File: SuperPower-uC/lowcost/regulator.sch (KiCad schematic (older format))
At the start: 23 parts, among them Q5 AO3401A, Q6 AO3401A, Q7 2N7002, U10 FP6291LR, U11 ME6210A33P, U12 ME6210A33P

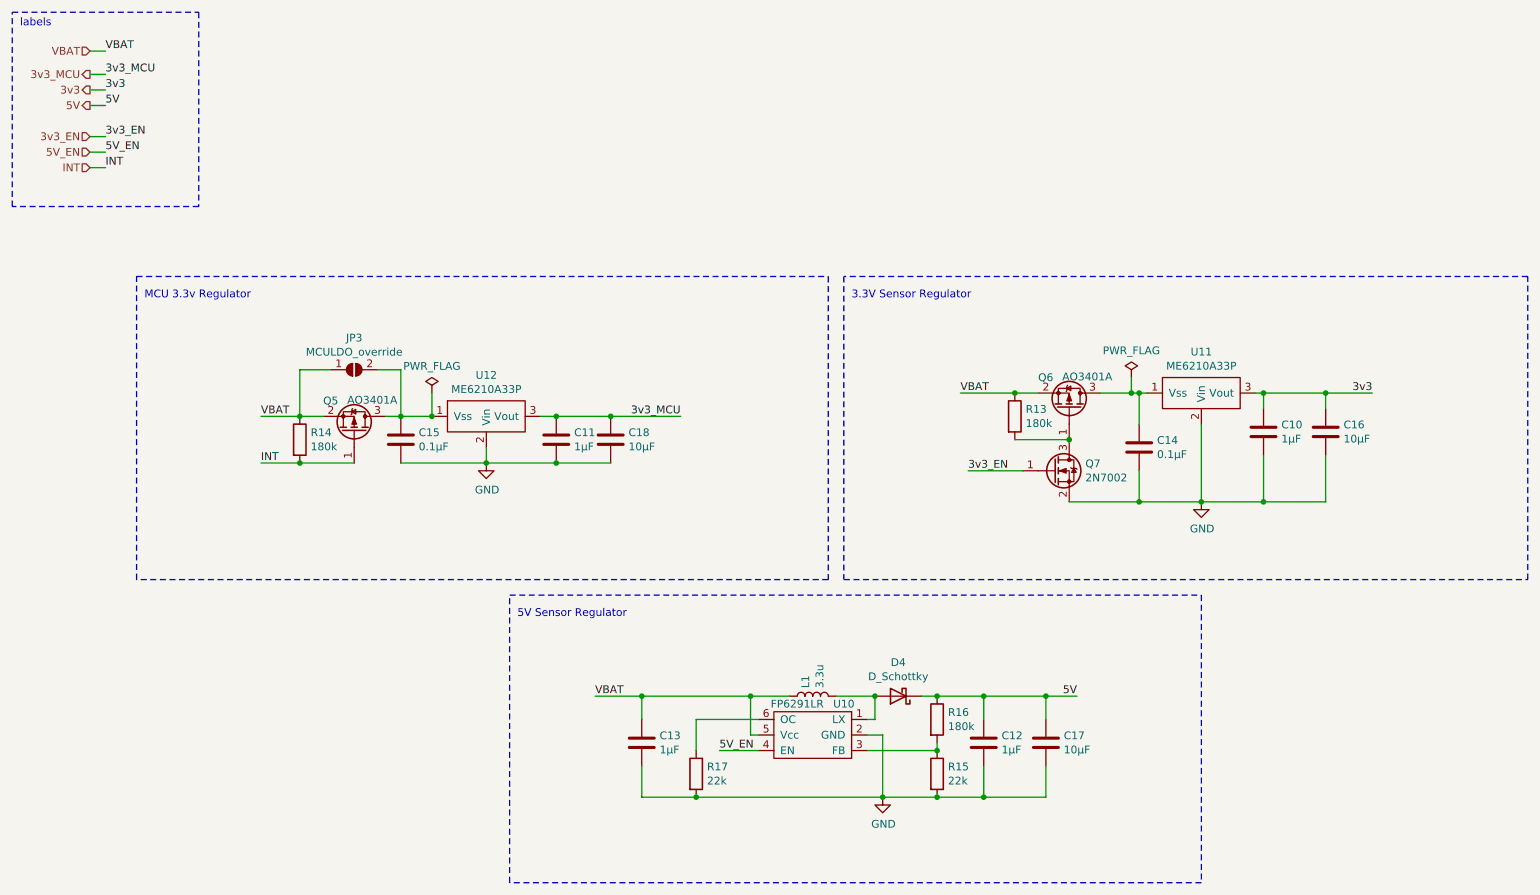
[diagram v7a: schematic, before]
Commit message: added 100R to protection ic and some minor other stuff
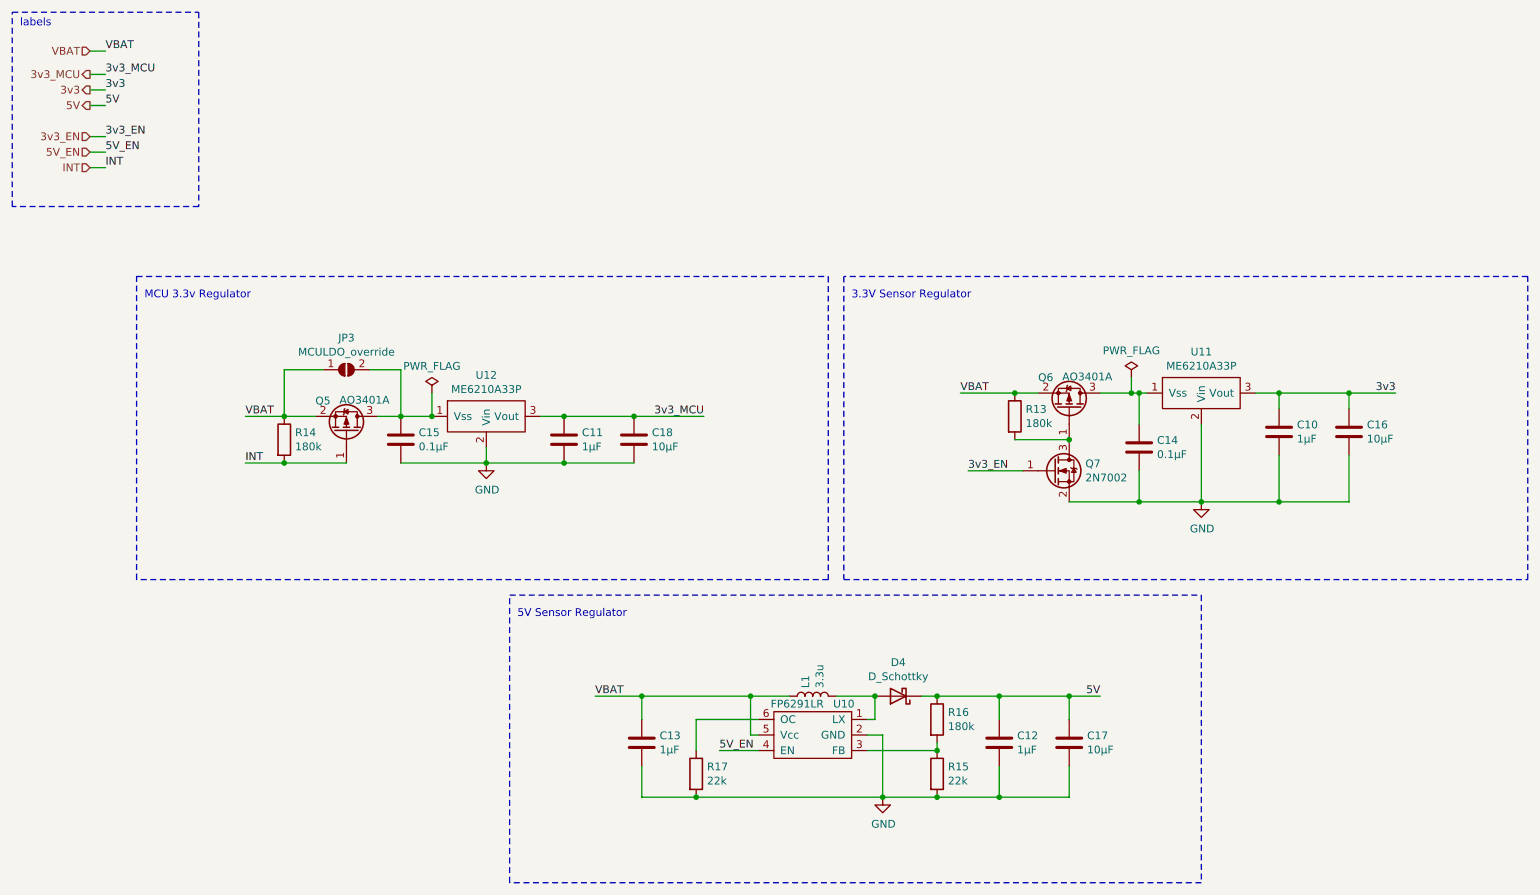
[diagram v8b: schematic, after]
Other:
- moved on the sheet: C10, C11, C12, C16, C17, C18, JP3, Q5, R14
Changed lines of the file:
@@
 L Transistor_FET:AO3401A Q5
 U 1 1 5F80895A
-P 2800 3300
-F 0 "Q5" V 3000 3100 50  0000 L CNN
-F 1 "AO3401A" V 3005 3255 50  0000 L CNN
-F 2 "Package_TO_SOT_SMD:SOT-23_Handsoldering" H 3000 3225 50  0001 L CIN
-F 3 "http://www.aosmd.com/pdfs/datasheet/AO3401A.pdf" H 2800 3300 50  0001 L CNN
-F 4 "C347476" H 2800 3300 50  0001 C CNN "LCSC"
-	1    2800 3300
+P 2750 3300
+F 0 "Q5" V 2950 3100 50  0000 L CNN
+F 1 "AO3401A" V 2955 3255 50  0000 L CNN
+F 2 "Package_TO_SOT_SMD:SOT-23_Handsoldering" H 2950 3225 50  0001 L CIN
+F 3 "http://www.aosmd.com/pdfs/datasheet/AO3401A.pdf" H 2750 3300 50  0001 L CNN
+F 4 "C347476" H 2750 3300 50  0001 C CNN "LCSC"
+	1    2750 3300
 	0    1    -1   0
 $EndComp
@@
 $EndComp
 Wire Wire Line
-	3000 3200 3100 3200
+	2950 3200 3100 3200
 Wire Wire Line
 	7600 3050 7800 3050
@@
 L Device:R R14
 U 1 1 5F8145C2
-P 2450 3350
-F 0 "R14" H 2520 3396 50  0000 L CNN
-F 1 "180k" H 2520 3305 50  0000 L CNN
-F 2 "Resistor_SMD:R_0603_1608Metric_Pad1.05x0.95mm_HandSolder" V 2380 3350 50  0001 C CNN
-F 3 "~" H 2450 3350 50  0001 C CNN
-F 4 "C22827" H 2450 3350 50  0001 C CNN "LCSC"
-	1    2450 3350
-	1    0    0    -1
-$EndComp
-Wire Wire Line
-	2600 3200 2450 3200
+P 2350 3350
+F 0 "R14" H 2420 3396 50  0000 L CNN
+F 1 "180k" H 2420 3305 50  0000 L CNN
+F 2 "Resistor_SMD:R_0603_1608Metric_Pad1.05x0.95mm_HandSolder" V 2280 3350 50  0001 C CNN
+F 3 "~" H 2350 3350 50  0001 C CNN
+F 4 "C22827" H 2350 3350 50  0001 C CNN "LCSC"
+	1    2350 3350
+	1    0    0    -1
+$EndComp
+Wire Wire Line
+	2550 3200 2350 3200
 $Comp
 L Transistor_FET:2N7002 Q7
@@
 L Device:C C10
 U 1 1 5F81F790
-P 8650 3300
-F 0 "C10" H 8765 3346 50  0000 L CNN
-F 1 "1µF" H 8765 3255 50  0000 L CNN
-F 2 "Capacitor_SMD:C_0603_1608Metric_Pad1.05x0.95mm_HandSolder" H 8688 3150 50  0001 C CNN
-F 3 "~" H 8650 3300 50  0001 C CNN
-F 4 "C15849" H 8650 3300 50  0001 C CNN "LCSC"
-	1    8650 3300
+P 8750 3300
+F 0 "C10" H 8865 3346 50  0000 L CNN
+F 1 "1µF" H 8865 3255 50  0000 L CNN
+F 2 "Capacitor_SMD:C_0603_1608Metric_Pad1.05x0.95mm_HandSolder" H 8788 3150 50  0001 C CNN
+F 3 "~" H 8750 3300 50  0001 C CNN
+F 4 "C15849" H 8750 3300 50  0001 C CNN "LCSC"
+	1    8750 3300
 	1    0    0    -1
 $EndComp
@@
 L Device:C C11
 U 1 1 5F822A09
-P 4100 3350
-F 0 "C11" H 4215 3396 50  0000 L CNN
-F 1 "1µF" H 4215 3305 50  0000 L CNN
-F 2 "Capacitor_SMD:C_0603_1608Metric_Pad1.05x0.95mm_HandSolder" H 4138 3200 50  0001 C CNN
-F 3 "~" H 4100 3350 50  0001 C CNN
-F 4 "C15849" H 4100 3350 50  0001 C CNN "LCSC"
-	1    4100 3350
-	1    0    0    -1
-$EndComp
-Connection ~ 4100 3200
-Wire Wire Line
-	4100 3200 4000 3200
-Wire Wire Line
-	4100 3500 3650 3500
+P 4150 3350
+F 0 "C11" H 4265 3396 50  0000 L CNN
+F 1 "1µF" H 4265 3305 50  0000 L CNN
+F 2 "Capacitor_SMD:C_0603_1608Metric_Pad1.05x0.95mm_HandSolder" H 4188 3200 50  0001 C CNN
+F 3 "~" H 4150 3350 50  0001 C CNN
+F 4 "C15849" H 4150 3350 50  0001 C CNN "LCSC"
+	1    4150 3350
+	1    0    0    -1
+$EndComp
+Connection ~ 4150 3200
 $Comp
 L Device:C C14
@@
 Wire Wire Line
 	7850 3750 7400 3750
-Connection ~ 2450 3200
-Wire Wire Line
-	2950 2900 3100 2900
+Connection ~ 2350 3200
+Wire Wire Line
+	2900 2900 3100 2900
 $Comp
 L Jumper:SolderJumper_2_Open JP3
 U 1 1 5F81FE3B
-P 2800 2900
-F 0 "JP3" H 2800 3105 50  0000 C CNN
-F 1 "MCULDO_override" H 2800 3014 50  0000 C CNN
-F 2 "Jumper:SolderJumper-2_P1.3mm_Open_Pad1.0x1.5mm" H 2800 2900 50  0001 C CNN
-F 3 "~" H 2800 2900 50  0001 C CNN
-	1    2800 2900
-	1    0    0    -1
-$EndComp
-Wire Wire Line
-	2450 2900 2450 3200
+P 2750 2900
+F 0 "JP3" H 2750 3105 50  0000 C CNN
+F 1 "MCULDO_override" H 2750 3014 50  0000 C CNN
+F 2 "Jumper:SolderJumper-2_P1.3mm_Open_Pad1.0x1.5mm" H 2750 2900 50  0001 C CNN
+F 3 "~" H 2750 2900 50  0001 C CNN
+	1    2750 2900
+	1    0    0    -1
+$EndComp
+Wire Wire Line
+	2350 2900 2350 3200
 Wire Wire Line
 	3100 2900 3100 3200
 Wire Wire Line
-	2450 2900 2650 2900
+	2350 2900 2600 2900
 $Comp
 L Device:C C16
 U 1 1 5F868BFD
-P 9050 3300
-F 0 "C16" H 9165 3346 50  0000 L CNN
-F 1 "10µF" H 9165 3255 50  0000 L CNN
-F 2 "Capacitor_SMD:C_0603_1608Metric_Pad1.05x0.95mm_HandSolder" H 9088 3150 50  0001 C CNN
-F 3 "~" H 9050 3300 50  0001 C CNN
-F 4 "C19702" H 9050 3300 50  0001 C CNN "LCSC"
-	1    9050 3300
+P 9200 3300
+F 0 "C16" H 9315 3346 50  0000 L CNN
+F 1 "10µF" H 9315 3255 50  0000 L CNN
+F 2 "Capacitor_SMD:C_0603_1608Metric_Pad1.05x0.95mm_HandSolder" H 9238 3150 50  0001 C CNN
+F 3 "~" H 9200 3300 50  0001 C CNN
+F 4 "C19702" H 9200 3300 50  0001 C CNN "LCSC"
+	1    9200 3300
 	1    0    0    -1
 $EndComp
@@
 	8250 3250 8250 3750
 Wire Wire Line
-	8250 3750 8650 3750
-Wire Wire Line
-	8600 3050 8650 3050
-Wire Wire Line
-	8650 3050 8650 3150
-Connection ~ 8650 3050
-Wire Wire Line
-	8650 3050 9050 3050
-Wire Wire Line
-	9050 3050 9050 3150
-Connection ~ 9050 3050
-Wire Wire Line
-	8650 3450 8650 3750
-Connection ~ 8650 3750
-Wire Wire Line
-	8650 3750 9050 3750
-Wire Wire Line
-	9050 3450 9050 3750
+	8250 3750 8750 3750
+Wire Wire Line
+	8600 3050 8750 3050
+Wire Wire Line
+	8750 3050 8750 3150
+Connection ~ 8750 3050
+Wire Wire Line
+	8750 3050 9200 3050
+Wire Wire Line
+	9200 3050 9200 3150
+Connection ~ 9200 3050
+Wire Wire Line
+	8750 3450 8750 3750
+Connection ~ 8750 3750
+Wire Wire Line
+	8750 3750 9200 3750
+Wire Wire Line
+	9200 3450 9200 3750
 $Comp
 L Device:C C18
 U 1 1 5F87C4EA
-P 4450 3350
-F 0 "C18" H 4565 3396 50  0000 L CNN
-F 1 "10µF" H 4565 3305 50  0000 L CNN
-F 2 "Capacitor_SMD:C_0603_1608Metric_Pad1.05x0.95mm_HandSolder" H 4488 3200 50  0001 C CNN
-F 3 "~" H 4450 3350 50  0001 C CNN
-F 4 "C19702" H 4450 3350 50  0001 C CNN "LCSC"
-	1    4450 3350
-	1    0    0    -1
-$EndComp
-Connection ~ 4450 3200
-Wire Wire Line
-	4100 3200 4450 3200
-Wire Wire Line
-	4450 3500 4100 3500
-Connection ~ 4100 3500
-Connection ~ 6850 5650
-Wire Wire Line
-	7250 5650 6850 5650
-Wire Wire Line
-	7250 5450 7250 5650
-Wire Wire Line
-	7250 5000 7250 5150
-Connection ~ 7250 5000
+P 4600 3350
+F 0 "C18" H 4715 3396 50  0000 L CNN
+F 1 "10µF" H 4715 3305 50  0000 L CNN
+F 2 "Capacitor_SMD:C_0603_1608Metric_Pad1.05x0.95mm_HandSolder" H 4638 3200 50  0001 C CNN
+F 3 "~" H 4600 3350 50  0001 C CNN
+F 4 "C19702" H 4600 3350 50  0001 C CNN "LCSC"
+	1    4600 3350
+	1    0    0    -1
+$EndComp
+Connection ~ 4600 3200
+Wire Wire Line
+	4600 3500 4150 3500
+Connection ~ 4150 3500
+Connection ~ 6950 5650
+Wire Wire Line
+	7400 5650 6950 5650
+Wire Wire Line
+	7400 5450 7400 5650
+Wire Wire Line
+	7400 5000 7400 5150
+Connection ~ 7400 5000
 $Comp
 L Device:C C17
 U 1 1 5F86990F
-P 7250 5300
-F 0 "C17" H 7365 5346 50  0000 L CNN
-F 1 "10µF" H 7365 5255 50  0000 L CNN
-F 2 "Capacitor_SMD:C_0603_1608Metric_Pad1.05x0.95mm_HandSolder" H 7288 5150 50  0001 C CNN
-F 3 "~" H 7250 5300 50  0001 C CNN
-F 4 "C19702" H 7250 5300 50  0001 C CNN "LCSC"
-	1    7250 5300
+P 7400 5300
+F 0 "C17" H 7515 5346 50  0000 L CNN
+F 1 "10µF" H 7515 5255 50  0000 L CNN
+F 2 "Capacitor_SMD:C_0603_1608Metric_Pad1.05x0.95mm_HandSolder" H 7438 5150 50  0001 C CNN
+F 3 "~" H 7400 5300 50  0001 C CNN
+F 4 "C19702" H 7400 5300 50  0001 C CNN "LCSC"
+	1    7400 5300
 	1    0    0    -1
 $EndComp
@@
 Connection ~ 6550 5650
 Wire Wire Line
-	6850 5650 6550 5650
-Wire Wire Line
-	6850 5450 6850 5650
-Wire Wire Line
-	6850 5000 7250 5000
-Connection ~ 6850 5000
-Wire Wire Line
-	6850 5000 6850 5150
+	6950 5650 6550 5650
+Wire Wire Line
+	6950 5450 6950 5650
+Wire Wire Line
+	6950 5000 7400 5000
+Connection ~ 6950 5000
+Wire Wire Line
+	6950 5000 6950 5150
 $Comp
 L Device:C C12
 U 1 1 5F84772B
-P 6850 5300
-F 0 "C12" H 6965 5346 50  0000 L CNN
-F 1 "1µF" H 6965 5255 50  0000 L CNN
-F 2 "Capacitor_SMD:C_0603_1608Metric_Pad1.05x0.95mm_HandSolder" H 6888 5150 50  0001 C CNN
-F 3 "~" H 6850 5300 50  0001 C CNN
-F 4 "C15849" H 6850 5300 50  0001 C CNN "LCSC"
-	1    6850 5300
+P 6950 5300
+F 0 "C12" H 7065 5346 50  0000 L CNN
+F 1 "1µF" H 7065 5255 50  0000 L CNN
+F 2 "Capacitor_SMD:C_0603_1608Metric_Pad1.05x0.95mm_HandSolder" H 6988 5150 50  0001 C CNN
+F 3 "~" H 6950 5300 50  0001 C CNN
+F 4 "C15849" H 6950 5300 50  0001 C CNN "LCSC"
+	1    6950 5300
 	1    0    0    -1
 $EndComp
@@
 $EndComp
 Wire Wire Line
-	6550 5000 6850 5000
+	6550 5000 6950 5000
 Wire Wire Line
 	6550 5350 6550 5300
@@
 Wire Wire Line
 	7050 3350 7400 3350
-Connection ~ 2450 3500
-Wire Wire Line
-	2450 3500 2800 3500
+Connection ~ 2350 3500
+Wire Wire Line
+	2350 3500 2750 3500
 Wire Notes Line
 	1400 2300 5850 2300
@@
 Text Label 1200 1600 0    50   ~ 0
 INT
-Text Label 2200 3200 0    50   ~ 0
+Text Label 2100 3200 0    50   ~ 0
 VBAT
-Text Label 4900 3200 2    50   ~ 0
+Text Label 5050 3200 2    50   ~ 0
 3v3_MCU
-Text Label 9350 3050 2    50   ~ 0
+Text Label 9500 3050 2    50   ~ 0
 3v3
 Text Label 6750 3550 0    50   ~ 0
@@
 Text Label 5150 5350 0    50   ~ 0
 5V_EN
-Text Label 2200 3500 0    50   ~ 0
+Text Label 2100 3500 0    50   ~ 0
 INT
-Text Label 7450 5000 2    50   ~ 0
+Text Label 7600 5000 2    50   ~ 0
 5V
 Text Label 6700 3050 0    50   ~ 0
@@
 	6700 3050 7050 3050
 Wire Wire Line
-	9050 3050 9350 3050
+	9200 3050 9500 3050
 Wire Wire Line
 	4350 5000 4650 5000
 Wire Wire Line
-	7250 5000 7450 5000
-Wire Wire Line
-	2200 3200 2450 3200
-Wire Wire Line
-	2200 3500 2450 3500
-Wire Wire Line
-	4450 3200 4900 3200
+	7400 5000 7600 5000
+Wire Wire Line
+	2100 3200 2350 3200
+Wire Wire Line
+	2100 3500 2350 3500
+Wire Wire Line
+	4600 3200 5050 3200
 Wire Wire Line
 	5150 5350 5400 5350
@@
 Text Notes 650  700  0    50   ~ 0
 labels\n
+Wire Wire Line
+	4150 3200 4600 3200
+Wire Wire Line
+	4000 3200 4150 3200
+Wire Wire Line
+	3650 3500 4150 3500
 $EndSCHEMATC
